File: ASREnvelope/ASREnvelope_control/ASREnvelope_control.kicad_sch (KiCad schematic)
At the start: 19 parts, among them J1 GATE, J3 OUT, J4 INV OUT, J5 Conn_01x06_Male, J6 Conn_01x04_Male, SW1 SW_SPDT

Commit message: work on power traces
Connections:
- net Conn1A: now also J6.2 (Pin_2); no longer J6.1 (Pin_1)
- net Conn3A: now also J5.5 (Pin_5), RV2.1, RV2.2, RV3.1, RV3.2; no longer J6.3 (Pin_3), R8.2
- net GND: now also J5.1 (Pin_1); no longer J6.2 (Pin_2)
- net GateJackA: now also J6.1 (Pin_1); no longer J5.1 (Pin_1)
- net Switch2A: now also J6.4 (Pin_4); no longer J5.5 (Pin_5)
- removed net Conn4A: J6.4 (Pin_4), RV2.1, RV2.2, RV3.1, RV3.2
- new net Conn2A: J6.3 (Pin_3), R8.2
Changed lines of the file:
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@@
     )
   )
-  (global_label "Conn4A" (shape input) (at 231.14 87.63 0) (fields_autoplaced)
+  (global_label "Conn3A" (shape input) (at 231.14 66.04 0) (fields_autoplaced)
     (effects (font (size 1.27 1.27)) (justify left))
-    (property "Intersheet References" "${INTERSHEET_REFS}" (id 0) (at 53.34 -36.83 0)
-      (effects (font (size 1.27 1.27)) hide)
+    (property "Intersheet References" "${INTERSHEET_REFS}" (id 0) (at 240.5683 65.9606 0)
+      (effects (font (size 1.27 1.27)) (justify left) hide)
     )
   )
@@
     )
   )
-  (global_label "Switch2A" (shape input) (at 231.14 66.04 0) (fields_autoplaced)
+  (global_label "Switch2A" (shape input) (at 231.14 87.63 0) (fields_autoplaced)
     (effects (font (size 1.27 1.27)) (justify left))
-    (property "Intersheet References" "${INTERSHEET_REFS}" (id 0) (at 76.2 -36.83 0)
+    (property "Intersheet References" "${INTERSHEET_REFS}" (id 0) (at 76.2 -15.24 0)
       (effects (font (size 1.27 1.27)) hide)
     )
   )
-  (global_label "GroundA" (shape input) (at 231.14 82.55 0) (fields_autoplaced)
+  (global_label "GroundA" (shape input) (at 231.14 55.88 0) (fields_autoplaced)
     (effects (font (size 1.27 1.27)) (justify left))
-    (property "Intersheet References" "${INTERSHEET_REFS}" (id 0) (at 53.34 -36.83 0)
+    (property "Intersheet References" "${INTERSHEET_REFS}" (id 0) (at 53.34 -63.5 0)
       (effects (font (size 1.27 1.27)) hide)
     )
@@
     )
   )
-  (global_label "Conn3A" (shape input) (at 231.14 85.09 0) (fields_autoplaced)
+  (global_label "Conn2A" (shape input) (at 231.14 85.09 0) (fields_autoplaced)
     (effects (font (size 1.27 1.27)) (justify left))
-    (property "Intersheet References" "${INTERSHEET_REFS}" (id 0) (at 53.34 -36.83 0)
-      (effects (font (size 1.27 1.27)) hide)
+    (property "Intersheet References" "${INTERSHEET_REFS}" (id 0) (at 240.5683 85.0106 0)
+      (effects (font (size 1.27 1.27)) (justify left) hide)
     )
   )
-  (global_label "Conn3A" (shape input) (at 158.75 39.37 180) (fields_autoplaced)
+  (global_label "Conn2A" (shape input) (at 158.75 39.37 180) (fields_autoplaced)
     (effects (font (size 1.27 1.27)) (justify right))
-    (property "Intersheet References" "${INTERSHEET_REFS}" (id 0) (at 82.55 -100.33 0)
-      (effects (font (size 1.27 1.27)) hide)
+    (property "Intersheet References" "${INTERSHEET_REFS}" (id 0) (at 149.3217 39.2906 0)
+      (effects (font (size 1.27 1.27)) (justify right) hide)
     )
   )
-  (global_label "GateJackA" (shape input) (at 231.14 55.88 0) (fields_autoplaced)
+  (global_label "GateJackA" (shape input) (at 231.14 80.01 0) (fields_autoplaced)
     (effects (font (size 1.27 1.27)) (justify left))
-    (property "Intersheet References" "${INTERSHEET_REFS}" (id 0) (at 76.2 -36.83 0)
+    (property "Intersheet References" "${INTERSHEET_REFS}" (id 0) (at 76.2 -12.7 0)
       (effects (font (size 1.27 1.27)) hide)
     )
@@
     )
   )
-  (global_label "Conn1A" (shape input) (at 231.14 80.01 0) (fields_autoplaced)
+  (global_label "Conn1A" (shape input) (at 231.14 82.55 0) (fields_autoplaced)
     (effects (font (size 1.27 1.27)) (justify left))
-    (property "Intersheet References" "${INTERSHEET_REFS}" (id 0) (at 53.34 -36.83 0)
+    (property "Intersheet References" "${INTERSHEET_REFS}" (id 0) (at 53.34 -34.29 0)
       (effects (font (size 1.27 1.27)) hide)
     )
@@
     )
   )
-  (global_label "Conn4A" (shape input) (at 205.74 39.37 0) (fields_autoplaced)
+  (global_label "Conn3A" (shape input) (at 205.74 39.37 0) (fields_autoplaced)
     (effects (font (size 1.27 1.27)) (justify left))
-    (property "Intersheet References" "${INTERSHEET_REFS}" (id 0) (at 82.55 -100.33 0)
-      (effects (font (size 1.27 1.27)) hide)
+    (property "Intersheet References" "${INTERSHEET_REFS}" (id 0) (at 215.1683 39.2906 0)
+      (effects (font (size 1.27 1.27)) (justify left) hide)
     )
   )

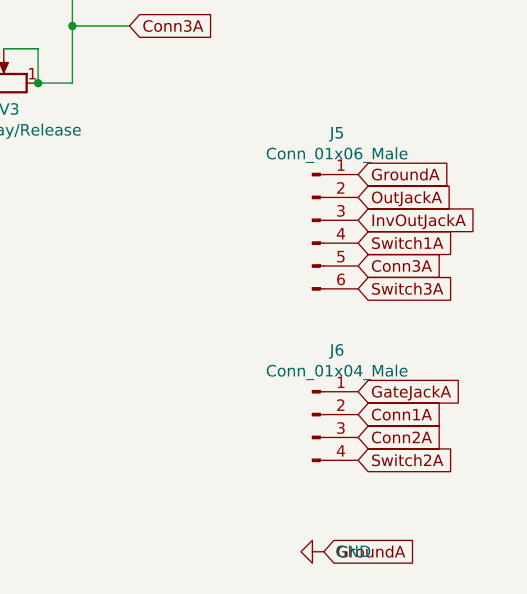
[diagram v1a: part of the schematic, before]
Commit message: fix control board connections
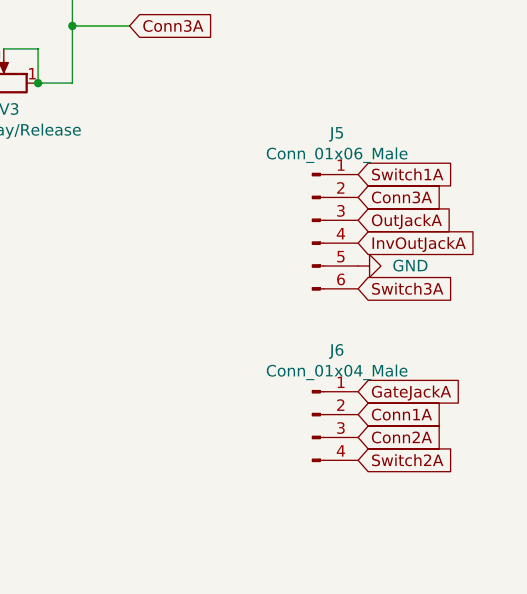
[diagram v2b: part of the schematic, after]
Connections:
- net Conn3A: now also J5.2 (Pin_2); no longer J5.5 (Pin_5)
- net GND: now also J5.5 (Pin_5); no longer J5.1 (Pin_1)
- net InvOutJackA: now also J5.4 (Pin_4); no longer J5.3 (Pin_3)
- net OutJackA: now also J5.3 (Pin_3); no longer J5.2 (Pin_2)
- net Switch1A: now also J5.1 (Pin_1); no longer J5.4 (Pin_4)
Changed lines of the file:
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@@
     )
   )
-  (global_label "Conn3A" (shape input) (at 231.14 66.04 0) (fields_autoplaced)
-    (effects (font (size 1.27 1.27)) (justify left))
-    (property "Intersheet References" "${INTERSHEET_REFS}" (id 0) (at 240.5683 65.9606 0)
+  (global_label "Conn3A" (shape input) (at 231.14 58.42 0) (fields_autoplaced)
+    (effects (font (size 1.27 1.27)) (justify left))
+    (property "Intersheet References" "${INTERSHEET_REFS}" (id 0) (at 240.5683 58.3406 0)
       (effects (font (size 1.27 1.27)) (justify left) hide)
     )
@@
     (effects (font (size 1.27 1.27)) (justify left))
     (property "Intersheet References" "${INTERSHEET_REFS}" (id 0) (at 76.2 -15.24 0)
-      (effects (font (size 1.27 1.27)) hide)
-    )
-  )
-  (global_label "GroundA" (shape input) (at 231.14 55.88 0) (fields_autoplaced)
-    (effects (font (size 1.27 1.27)) (justify left))
-    (property "Intersheet References" "${INTERSHEET_REFS}" (id 0) (at 53.34 -63.5 0)
       (effects (font (size 1.27 1.27)) hide)
     )
@@
     )
   )
-  (global_label "Switch1A" (shape input) (at 231.14 63.5 0) (fields_autoplaced)
-    (effects (font (size 1.27 1.27)) (justify left))
-    (property "Intersheet References" "${INTERSHEET_REFS}" (id 0) (at 76.2 -36.83 0)
+  (global_label "Switch1A" (shape input) (at 231.14 55.88 0) (fields_autoplaced)
+    (effects (font (size 1.27 1.27)) (justify left))
+    (property "Intersheet References" "${INTERSHEET_REFS}" (id 0) (at 76.2 -44.45 0)
       (effects (font (size 1.27 1.27)) hide)
     )
@@
     )
   )
-  (global_label "InvOutJackA" (shape input) (at 231.14 60.96 0) (fields_autoplaced)
-    (effects (font (size 1.27 1.27)) (justify left))
-    (property "Intersheet References" "${INTERSHEET_REFS}" (id 0) (at 76.2 -36.83 0)
-      (effects (font (size 1.27 1.27)) hide)
-    )
-  )
-  (global_label "GroundA" (shape input) (at 227.33 97.79 0) (fields_autoplaced)
-    (effects (font (size 1.27 1.27)) (justify left))
-    (property "Intersheet References" "${INTERSHEET_REFS}" (id 0) (at 53.34 -41.91 0)
+  (global_label "InvOutJackA" (shape input) (at 231.14 63.5 0) (fields_autoplaced)
+    (effects (font (size 1.27 1.27)) (justify left))
+    (property "Intersheet References" "${INTERSHEET_REFS}" (id 0) (at 76.2 -34.29 0)
       (effects (font (size 1.27 1.27)) hide)
     )
@@
     )
   )
-  (global_label "OutJackA" (shape input) (at 231.14 58.42 0) (fields_autoplaced)
-    (effects (font (size 1.27 1.27)) (justify left))
-    (property "Intersheet References" "${INTERSHEET_REFS}" (id 0) (at 76.2 -36.83 0)
+  (global_label "OutJackA" (shape input) (at 231.14 60.96 0) (fields_autoplaced)
+    (effects (font (size 1.27 1.27)) (justify left))
+    (property "Intersheet References" "${INTERSHEET_REFS}" (id 0) (at 76.2 -34.29 0)
       (effects (font (size 1.27 1.27)) hide)
     )
@@
     (pin "1")
   )
-  (symbol (lib_id "power:GND") (at 227.33 97.79 270) (unit 1)
-    (in_bom yes) (on_board yes) (fields_autoplaced)
-    (property "Reference" "#PWR?" (id 0) (at 220.98 97.79 0)
-      (effects (font (size 1.27 1.27)) hide)
-    )
-    (property "Value" "GND" (id 1) (at 228.6 97.7899 90)
-      (effects (font (size 1.27 1.27)) (justify left))
-    )
-    (property "Footprint" "" (id 2) (at 227.33 97.79 0)
-      (effects (font (size 1.27 1.27)) hide)
-    )
-    (property "Datasheet" "" (id 3) (at 227.33 97.79 0)
-      (effects (font (size 1.27 1.27)) hide)
-    )
+  (symbol (lib_id "power:GND") (at 231.14 66.04 90) (unit 1)
+    (in_bom yes) (on_board yes) (fields_autoplaced)
+    (property "Reference" "#PWR?" (id 0) (at 237.49 66.04 0)
+      (effects (font (size 1.27 1.27)) hide)
+    )
+    (property "Value" "GND" (id 1) (at 234.95 66.0399 90)
+      (effects (font (size 1.27 1.27)) (justify right))
+    )
+    (property "Footprint" "" (id 2) (at 231.14 66.04 0)
+      (effects (font (size 1.27 1.27)) hide)
+    )
+    (property "Datasheet" "" (id 3) (at 231.14 66.04 0)
+      (effects (font (size 1.27 1.27)) hide)
+    )

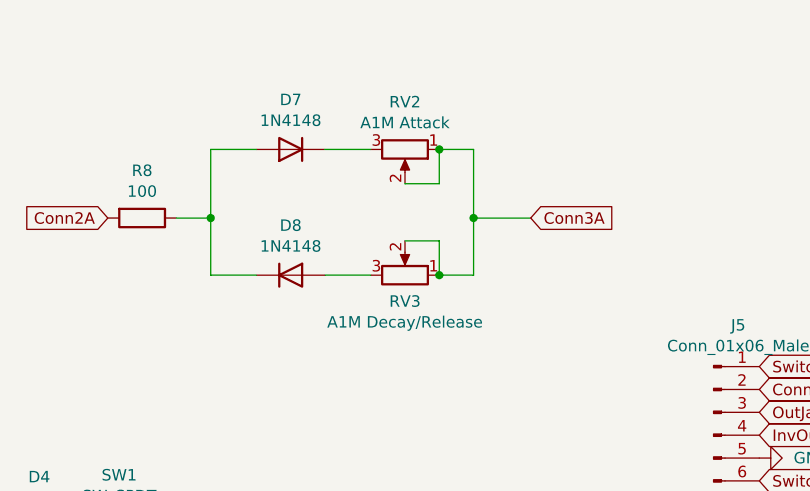
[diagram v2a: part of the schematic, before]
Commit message: finish control traces
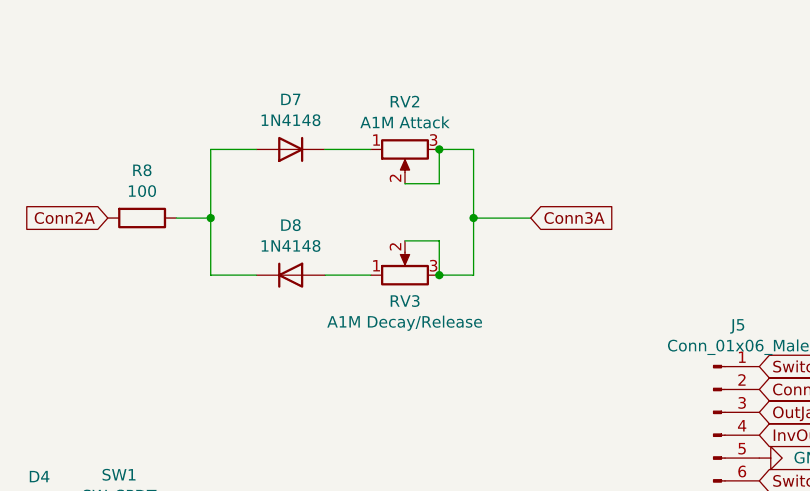
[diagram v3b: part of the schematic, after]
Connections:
- net Conn3A: now also RV2.3, RV3.3; no longer RV2.1, RV3.1
- net at D7.1 (K): now also RV2.1; no longer RV2.3
- net at D8.2 (A): now also RV3.1; no longer RV3.3
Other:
- moved on the sheet: RV2, RV3
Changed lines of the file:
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@@
     (pin "6")
   )
-  (symbol (lib_id "ASREnvelope-rescue:R_POT-Device") (at 191.77 31.75 270) (unit 1)
+  (symbol (lib_id "ASREnvelope-rescue:R_POT-Device") (at 191.77 31.75 90) (mirror x) (unit 1)
     (in_bom yes) (on_board yes)
     (property "Reference" "RV2" (id 0) (at 191.77 26.4922 90))
@@
     (pin "3")
   )
-  (symbol (lib_id "ASREnvelope-rescue:R_POT-Device") (at 191.77 45.72 270) (mirror x) (unit 1)
+  (symbol (lib_id "ASREnvelope-rescue:R_POT-Device") (at 191.77 45.72 90) (unit 1)
     (in_bom yes) (on_board yes)
     (property "Reference" "RV3" (id 0) (at 191.77 48.641 90))
@@
   (symbol (lib_id "power:GND") (at 58.42 74.93 270) (unit 1)
     (in_bom yes) (on_board yes) (fields_autoplaced)
-    (property "Reference" "#PWR?" (id 0) (at 52.07 74.93 0)
+    (property "Reference" "#PWR0105" (id 0) (at 52.07 74.93 0)
       (effects (font (size 1.27 1.27)) hide)
     )
@@
   (symbol (lib_id "power:GND") (at 58.42 92.71 270) (unit 1)
     (in_bom yes) (on_board yes) (fields_autoplaced)
-    (property "Reference" "#PWR?" (id 0) (at 52.07 92.71 0)
+    (property "Reference" "#PWR0106" (id 0) (at 52.07 92.71 0)
       (effects (font (size 1.27 1.27)) hide)
     )
@@
   (symbol (lib_id "power:GND") (at 52.07 48.26 90) (unit 1)
     (in_bom yes) (on_board yes) (fields_autoplaced)
-    (property "Reference" "#PWR?" (id 0) (at 58.42 48.26 0)
+    (property "Reference" "#PWR0104" (id 0) (at 58.42 48.26 0)
       (effects (font (size 1.27 1.27)) hide)
     )
@@
   (symbol (lib_id "power:GND") (at 52.07 53.34 90) (unit 1)
     (in_bom yes) (on_board yes) (fields_autoplaced)
-    (property "Reference" "#PWR?" (id 0) (at 58.42 53.34 0)
+    (property "Reference" "#PWR0103" (id 0) (at 58.42 53.34 0)
       (effects (font (size 1.27 1.27)) hide)
     )
@@
   (symbol (lib_id "power:GND") (at 154.94 93.98 0) (unit 1)
     (in_bom yes) (on_board yes) (fields_autoplaced)
-    (property "Reference" "#PWR?" (id 0) (at 154.94 100.33 0)
+    (property "Reference" "#PWR0107" (id 0) (at 154.94 100.33 0)
       (effects (font (size 1.27 1.27)) hide)
     )
@@
   (symbol (lib_id "power:GND") (at 231.14 66.04 90) (unit 1)
     (in_bom yes) (on_board yes) (fields_autoplaced)
-    (property "Reference" "#PWR?" (id 0) (at 237.49 66.04 0)
+    (property "Reference" "#PWR0101" (id 0) (at 237.49 66.04 0)
       (effects (font (size 1.27 1.27)) hide)
     )
@@
   (symbol (lib_id "power:GND") (at 130.81 50.8 90) (unit 1)
     (in_bom yes) (on_board yes) (fields_autoplaced)
-    (property "Reference" "#PWR?" (id 0) (at 137.16 50.8 0)
+    (property "Reference" "#PWR0102" (id 0) (at 137.16 50.8 0)
       (effects (font (size 1.27 1.27)) hide)
     )
@@
   )
   (symbol_instances
+    (path "/ed33e7a3-a000-445e-b41a-1bf1ef20e0b5"
+      (reference "#PWR0101") (unit 1) (value "GND") (footprint "")
+    )
+    (path "/ed52bb3c-e2cb-41f7-aea3-030e62c2aa39"
+      (reference "#PWR0102") (unit 1) (value "GND") (footprint "")
+    )
+    (path "/bb11cb2e-d443-4ba1-a3e1-30e4d6fb632d"
+      (reference "#PWR0103") (unit 1) (value "GND") (footprint "")
+    )
+    (path "/7a64658c-9c43-45b8-96f7-9990527c4990"
+      (reference "#PWR0104") (unit 1) (value "GND") (footprint "")
+    )
     (path "/35d9f3d9-cc06-432d-b407-d240bc4b0369"
-      (reference "#PWR?") (unit 1) (value "GND") (footprint "")
+      (reference "#PWR0105") (unit 1) (value "GND") (footprint "")
     )
     (path "/6580fc95-04cd-47c3-9002-45267db36abc"
-      (reference "#PWR?") (unit 1) (value "GND") (footprint "")
-    )
-    (path "/7a64658c-9c43-45b8-96f7-9990527c4990"
-      (reference "#PWR?") (unit 1) (value "GND") (footprint "")
-    )
-    (path "/bb11cb2e-d443-4ba1-a3e1-30e4d6fb632d"
-      (reference "#PWR?") (unit 1) (value "GND") (footprint "")
+      (reference "#PWR0106") (unit 1) (value "GND") (footprint "")
     )
     (path "/bd71d48e-6b0b-46bf-9740-a56808289fd3"
-      (reference "#PWR?") (unit 1) (value "GND") (footprint "")
-    )
-    (path "/ed33e7a3-a000-445e-b41a-1bf1ef20e0b5"
-      (reference "#PWR?") (unit 1) (value "GND") (footprint "")
-    )
-    (path "/ed52bb3c-e2cb-41f7-aea3-030e62c2aa39"
-      (reference "#PWR?") (unit 1) (value "GND") (footprint "")
+      (reference "#PWR0107") (unit 1) (value "GND") (footprint "")
     )
     (path "/00000000-0000-0000-0000-000062d84a38"
